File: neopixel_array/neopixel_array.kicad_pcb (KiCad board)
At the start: 2 copper layers, 153 x 146 mm, 77 parts, among them J1 Conn_01x10

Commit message: Ordered the PCB using the gerber files
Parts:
- removed 3M (x4): MountingHole_3.2mm_M3, MountingHole:MountingHole_3.2mm_M3
- added M2.5: MountingHole_2.5mm, MountingHole:MountingHole_2.5mm, F.Cu at (72.5, 30.0)
- added M2.5: MountingHole_2.5mm, MountingHole:MountingHole_2.5mm, F.Cu at (72.5, 157.0)
- added M2.5: MountingHole_2.5mm, MountingHole:MountingHole_2.5mm, F.Cu at (212.0, 157.0)
- added M2.5: MountingHole_2.5mm, MountingHole:MountingHole_2.5mm, F.Cu at (213.5, 30.0)
- moved C15 0.50 mm to (136.5, 81.0)
- moved C21 0.50 mm to (162.0, 81.0)
- moved C3 0.50 mm to (85.5, 81.0)
- moved C9 0.50 mm to (111.5, 81.0)
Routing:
- net GND: track 227.6 -> 229.5 mm
- added copper zone on F.Cu, net +5V
- added copper zone on B.Cu, net GND
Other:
- board size 153 x 146 mm -> 147 x 146 mm

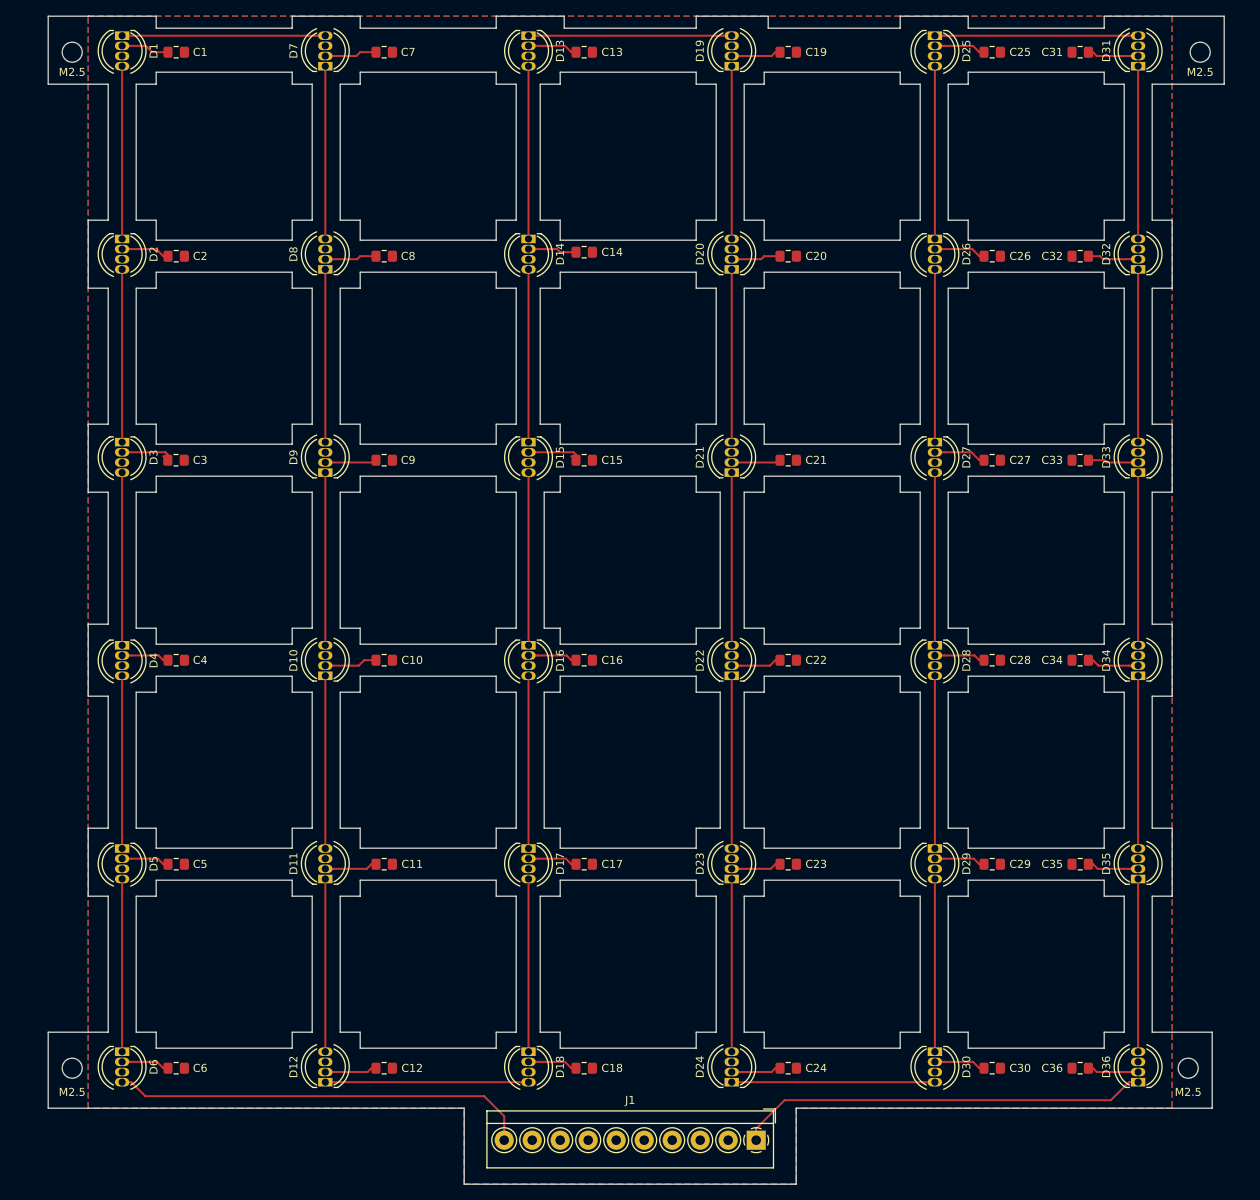
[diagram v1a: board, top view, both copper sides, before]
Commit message: updated pcb with svg files
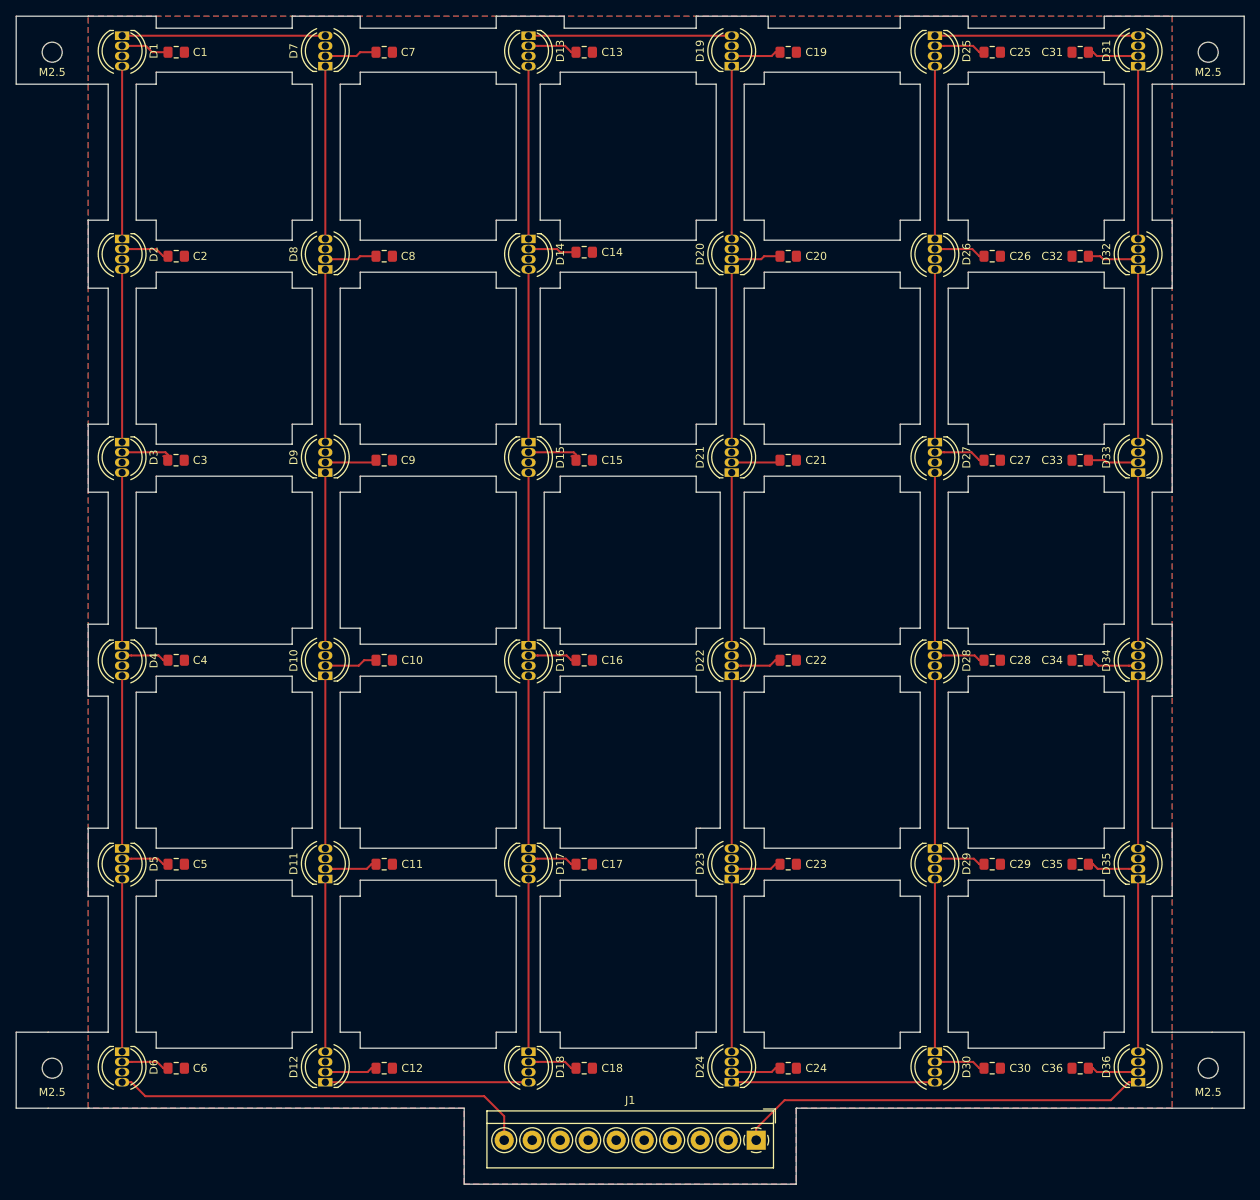
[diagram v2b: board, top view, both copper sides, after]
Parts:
- moved M2.5 2.50 mm to (70.0, 30.0)
- moved M2.5 2.50 mm to (70.0, 157.0)
- moved M2.5 2.50 mm to (214.5, 157.0)
- moved M2.5 1.00 mm to (214.5, 30.0)
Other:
- board size 147 x 146 mm -> 153.5 x 146 mm
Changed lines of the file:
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@@
   (general
     (thickness 1.6)
-    (drawings 377)
+    (drawings 383)
     (tracks 177)
     (zones 0)
@@
     (visible_elements FFFDF77F)
     (pcbplotparams
-      (layerselection 0x010f0_ffffffff)
+      (layerselection 0x01040_7ffffffe)
       (usegerberextensions false)
       (usegerberattributes false)
       (usegerberadvancedattributes false)
       (creategerberjobfile false)
-      (excludeedgelayer true)
+      (excludeedgelayer false)
       (linewidth 0.100000)
       (plotframeref false)
@@
       (padsonsilk false)
       (subtractmaskfromsilk false)
-      (outputformat 1)
+      (outputformat 5)
       (mirror false)
-      (drillshape 0)
+      (drillshape 2)
       (scaleselection 1)
       (outputdirectory ""))
@@
   )
   (module MountingHole:MountingHole_2.5mm (layer F.Cu)
-    (at 72.5 30)
+    (at 70 30)
     (descr "Mounting Hole 2.5mm, no annular")
     (tags "mounting hole 2.5mm no annular")
@@
     (pad 1 np_thru_hole circle (at 0 0) (size 2.5 2.5) (drill 2.5) (layers *.Cu *.Mask))
   )
-  (module MountingHole:MountingHole_2.5mm (layer F.Cu)
-    (at 72.5 157)
+  (module MountingHole:MountingHole_2.5mm locked (layer F.Cu)
+    (at 70 157)
     (descr "Mounting Hole 2.5mm, no annular")
     (tags "mounting hole 2.5mm no annular")
@@
   )
   (module MountingHole:MountingHole_2.5mm (layer F.Cu)
-    (at 212 157)
+    (at 214.5 157)
     (descr "Mounting Hole 2.5mm, no annular")
     (tags "mounting hole 2.5mm no annular")
@@
   )
   (module MountingHole:MountingHole_2.5mm (layer F.Cu)
-    (at 213.5 30)
+    (at 214.5 30)
     (descr "Mounting Hole 2.5mm, no annular")
     (tags "mounting hole 2.5mm no annular")
@@
     )
   )
+  (dimension 153.5 (width 0.12) (layer F.SilkS)
+    (gr_text "153.500 mm" (at 142.25 19.73) (layer F.SilkS)
+      (effects (font (size 1 1) (thickness 0.15)))
+    )
+    (feature1 (pts (xy 219 25.5) (xy 219 20.413579)))
+    (feature2 (pts (xy 65.5 25.5) (xy 65.5 20.413579)))
+    (crossbar (pts (xy 65.5 21) (xy 219 21)))
+    (arrow1a (pts (xy 219 21) (xy 217.873496 21.586421)))
+    (arrow1b (pts (xy 219 21) (xy 217.873496 20.413579)))
+    (arrow2a (pts (xy 65.5 21) (xy 66.626504 21.586421)))
+    (arrow2b (pts (xy 65.5 21) (xy 66.626504 20.413579)))
+  )
+  (dimension 136.5 (width 0.12) (layer F.SilkS)
+    (gr_text "136.500 mm" (at 57.73 93.75 90) (layer F.SilkS)
+      (effects (font (size 1 1) (thickness 0.15)))
+    )
+    (feature1 (pts (xy 65.5 25.5) (xy 58.413579 25.5)))
+    (feature2 (pts (xy 65.5 162) (xy 58.413579 162)))
+    (crossbar (pts (xy 59 162) (xy 59 25.5)))
+    (arrow1a (pts (xy 59 25.5) (xy 59.586421 26.626504)))
+    (arrow1b (pts (xy 59 25.5) (xy 58.413579 26.626504)))
+    (arrow2a (pts (xy 59 162) (xy 59.586421 160.873496)))
+    (arrow2b (pts (xy 59 162) (xy 58.413579 160.873496)))
+  )
+  (gr_line (start 215 162) (end 219 162) (layer Edge.Cuts) (width 0.05))
+  (gr_line (start 219 152.5) (end 219 162) (layer Edge.Cuts) (width 0.05))
+  (gr_line (start 215 152.5) (end 219 152.5) (layer Edge.Cuts) (width 0.05))
+  (gr_line (start 69.5 162) (end 65.5 162) (layer Edge.Cuts) (width 0.05))
+  (gr_line (start 65.5 152.5) (end 65.5 162) (layer Edge.Cuts) (width 0.05))
+  (gr_line (start 69.5 152.5) (end 65.5 152.5) (layer Edge.Cuts) (width 0.05))
   (gr_line (start 151 127) (end 150.5 127) (layer Edge.Cuts) (width 0.05))
   (gr_line (start 184.5 129.5) (end 201.5 129.5) (layer Edge.Cuts) (width 0.05))
@@
   (gr_line (start 201.5 79) (end 201.5 76.5) (layer Edge.Cuts) (width 0.05))
   (gr_line (start 184.5 83) (end 184.5 85) (layer Edge.Cuts) (width 0.05))
-  (gr_line (start 69.5 34) (end 74.5 34) (layer Edge.Cuts) (width 0.05))
-  (gr_line (start 69.5 25.5) (end 69.5 34) (layer Edge.Cuts) (width 0.05))
-  (gr_line (start 74.5 25.5) (end 69.5 25.5) (layer Edge.Cuts) (width 0.05))
+  (gr_line (start 65.5 34) (end 74.5 34) (layer Edge.Cuts) (width 0.05))
+  (gr_line (start 65.5 25.5) (end 65.5 34) (layer Edge.Cuts) (width 0.05))
+  (gr_line (start 74.5 25.5) (end 65.5 25.5) (layer Edge.Cuts) (width 0.05))
   (gr_line (start 69.5 162) (end 74.5 162) (layer Edge.Cuts) (width 0.05))
-  (gr_line (start 69.5 152.5) (end 69.5 162) (layer Edge.Cuts) (width 0.05))
   (gr_line (start 74.5 152.5) (end 69.5 152.5) (layer Edge.Cuts) (width 0.05))
   (gr_line (start 215 162) (end 210 162) (layer Edge.Cuts) (width 0.05))
-  (gr_line (start 215 152.5) (end 215 162) (layer Edge.Cuts) (width 0.05))
   (gr_line (start 210 152.5) (end 215 152.5) (layer Edge.Cuts) (width 0.05))
-  (gr_line (start 216.5 25.5) (end 210 25.5) (layer Edge.Cuts) (width 0.05))
-  (gr_line (start 216.5 34) (end 216.5 25.5) (layer Edge.Cuts) (width 0.05))
-  (gr_line (start 210 34) (end 216.5 34) (layer Edge.Cuts) (width 0.05))
+  (gr_line (start 219 25.5) (end 210 25.5) (layer Edge.Cuts) (width 0.05))
+  (gr_line (start 219 34) (end 219 25.5) (layer Edge.Cuts) (width 0.05))
+  (gr_line (start 210 34) (end 219 34) (layer Edge.Cuts) (width 0.05))
   (gr_line (start 163 162) (end 210 162) (layer Edge.Cuts) (width 0.05))
   (gr_line (start 121.5 162) (end 74.5 162) (layer Edge.Cuts) (width 0.05))
